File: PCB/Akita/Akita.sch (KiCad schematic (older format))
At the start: 0 parts

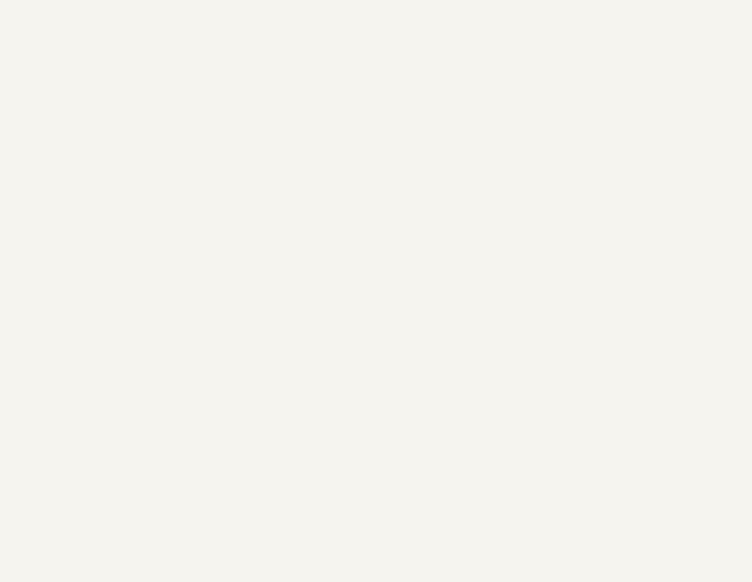
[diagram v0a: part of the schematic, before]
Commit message: Parts
Rudimentary scheamtic srtructure laid out, FPGA parts put on sheet. Basic passive components for FPGA selected and added to project library.
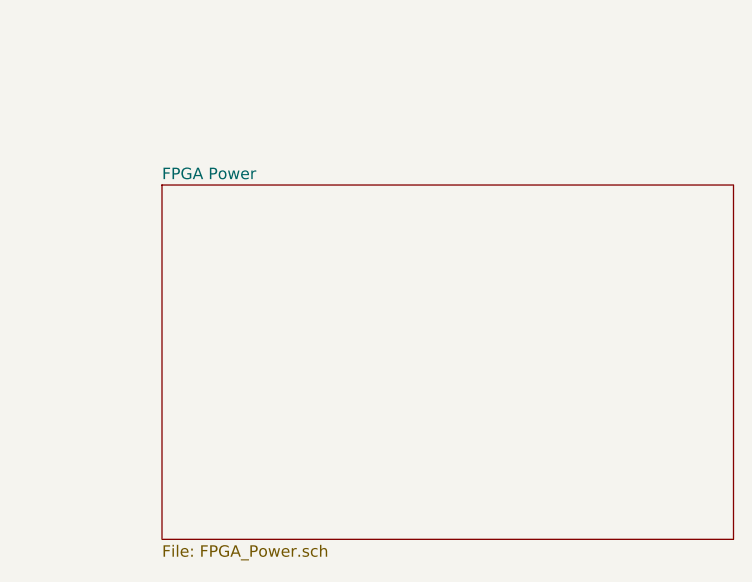
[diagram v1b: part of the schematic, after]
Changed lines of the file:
@@
 EESchema Schematic File Version 4
+LIBS:Akita-cache
 EELAYER 29 0
 EELAYER END
 $Descr A4 11693 8268
 encoding utf-8
-Sheet 1 6
+Sheet 1 7
 Title ""
 Date ""
@@
 F1 "IO.sch" 50
 $EndSheet
+$Sheet
+S 7500 4000 2500 1550
+U 5CDC6050
+F0 "FPGA Power" 50
+F1 "FPGA_Power.sch" 50
+$EndSheet
 $EndSCHEMATC
